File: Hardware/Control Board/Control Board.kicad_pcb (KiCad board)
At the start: 4 copper layers, 49.7 x 30 mm, 82 parts, among them J101 B4B-XH-A, J102 SWD, J103 UART, J104 Button, J105 Symbol Light, J106 X Light, J107 B Light, J108 O Light, J109 X Light, SW101 PTS636 SL43 SMTR LFS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

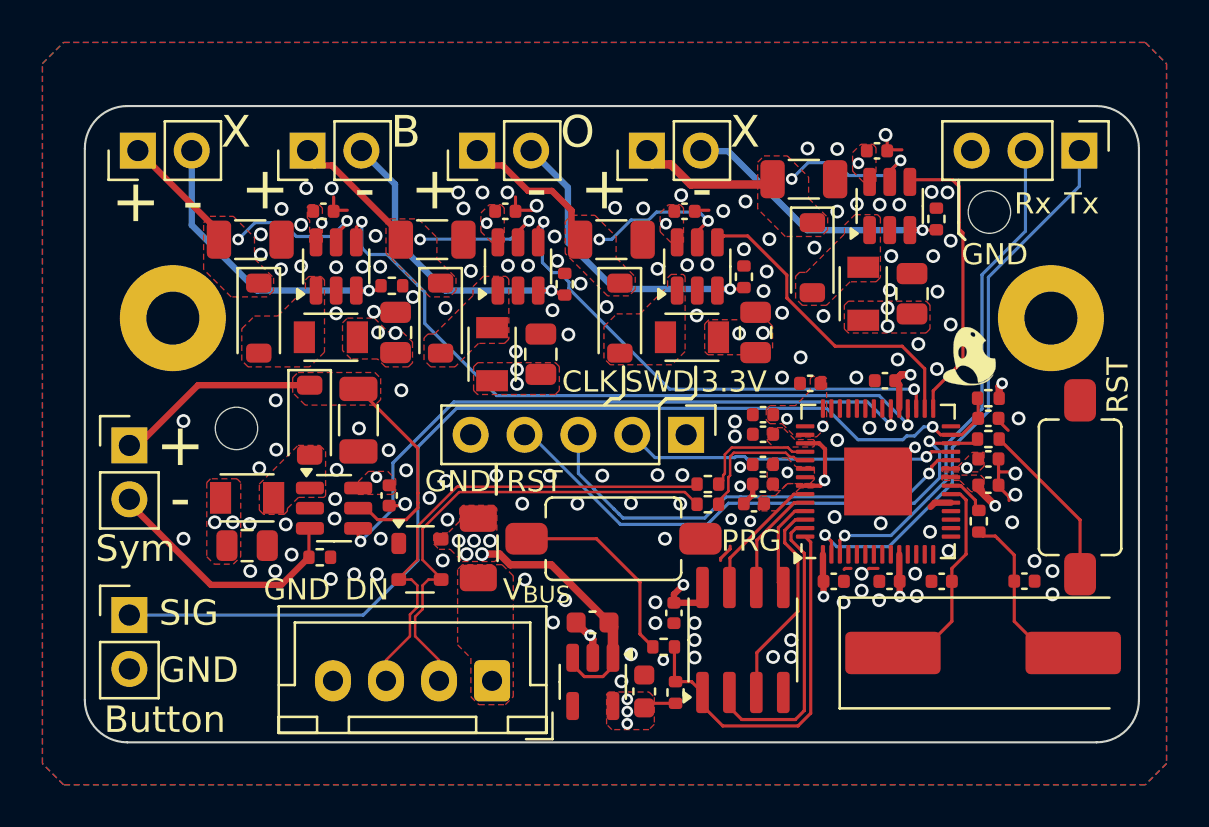
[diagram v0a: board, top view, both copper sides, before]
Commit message: Added stiching vias, 3D models
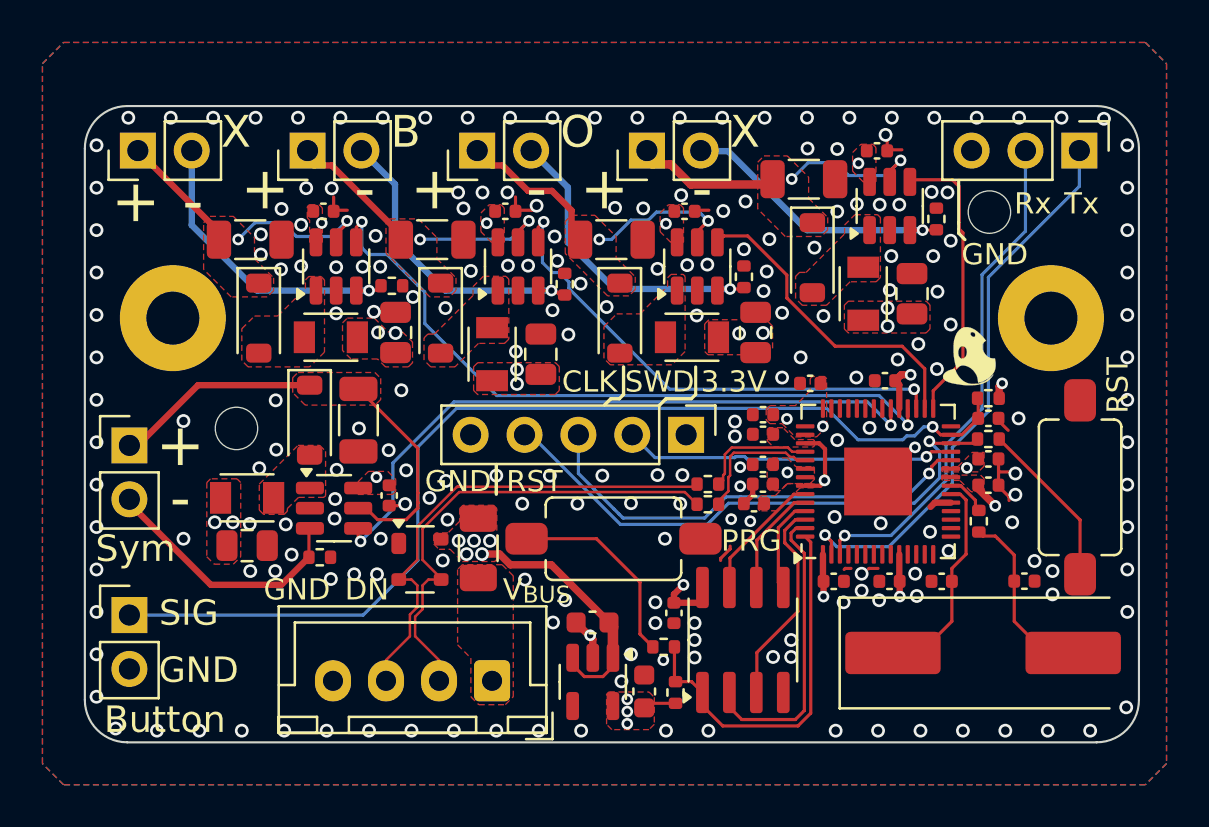
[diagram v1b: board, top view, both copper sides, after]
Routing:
- net GND: vias 145 -> 217
